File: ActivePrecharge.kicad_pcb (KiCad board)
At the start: 2 copper layers, 71 x 55 mm, 34 parts, among them Con1 LED, J1 Conn_01x03, J2 Conn_01x02, J3 Conn_01x02, Q1 IRLML0030, U1 NCP785AH50T1G, U2 NCP785AH50T1G, U3 TLV9301xDCK, U4 TCMT1106

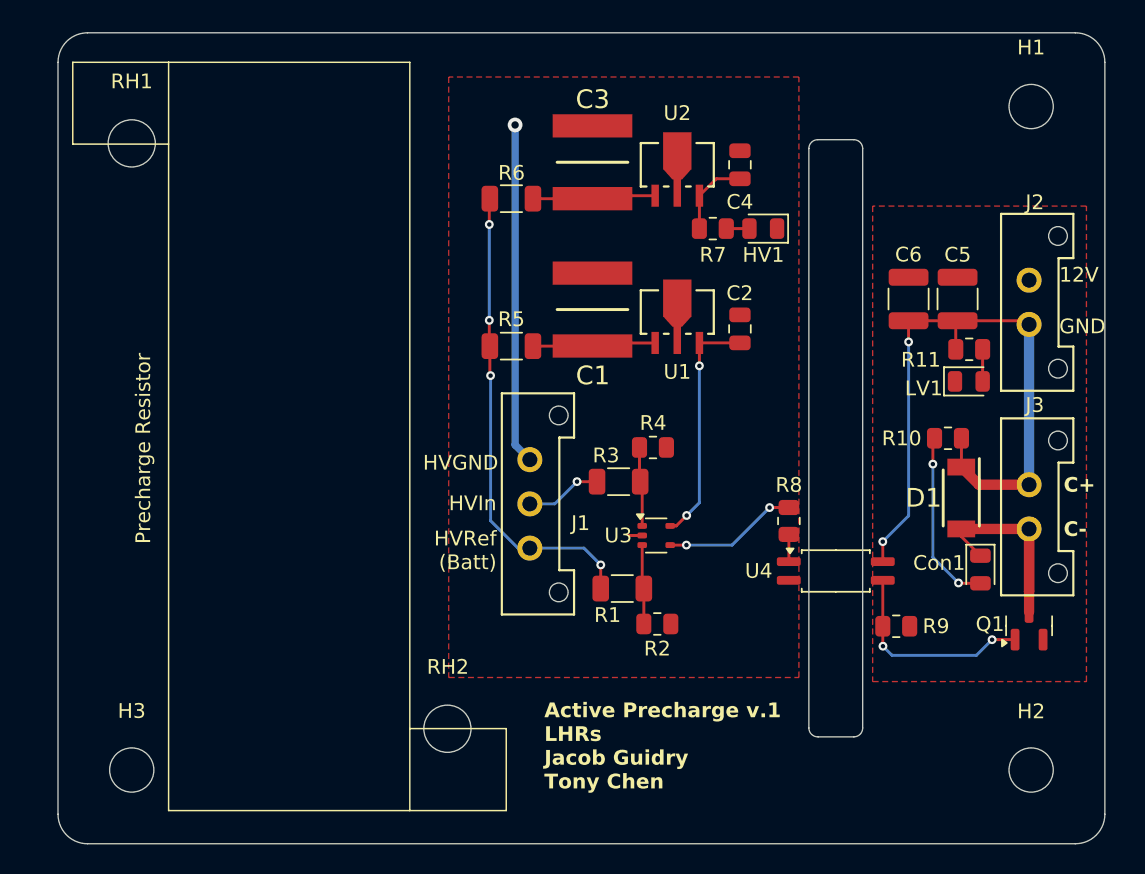
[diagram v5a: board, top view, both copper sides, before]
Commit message: refix HVGND isolation issue
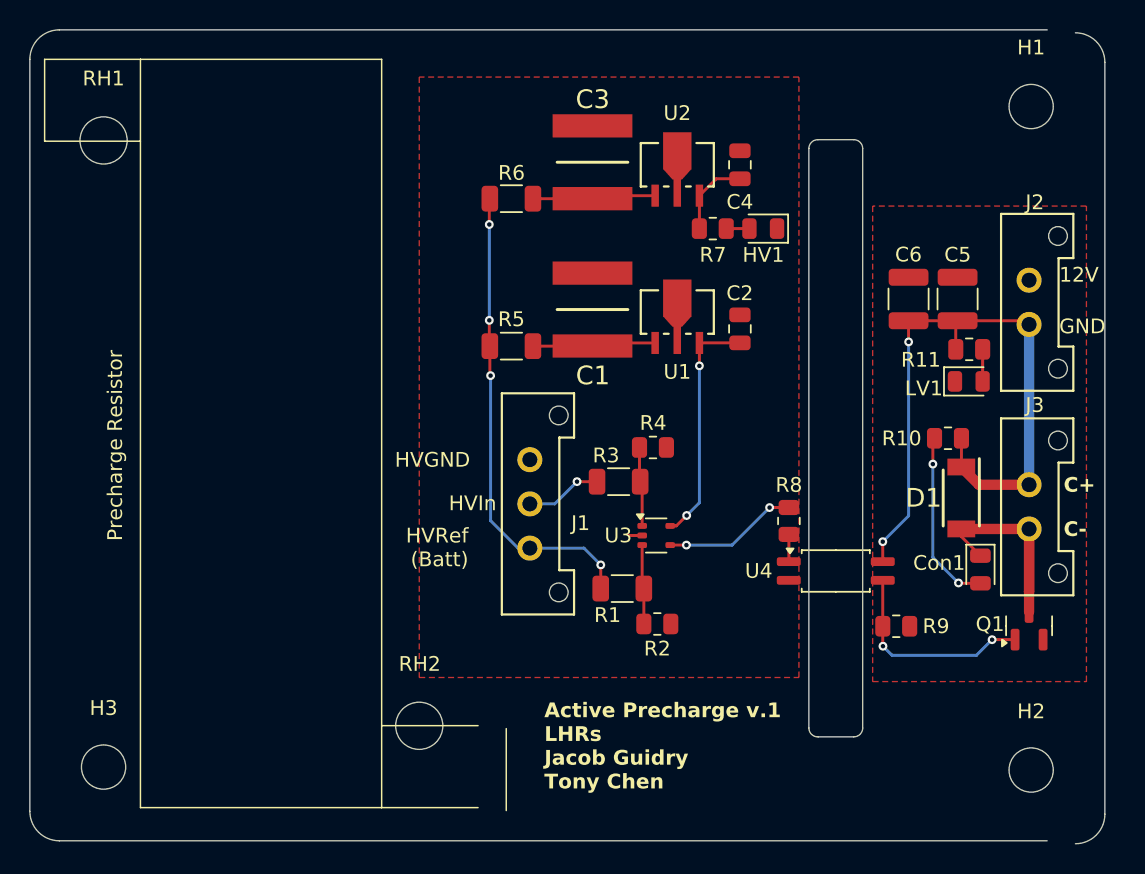
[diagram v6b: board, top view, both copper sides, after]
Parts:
- moved H3 1.92 mm to (77.6, 117.8)
- moved RH1 1.92 mm to (77.6, 75.3)
- moved RH2 1.92 mm to (99.0, 115.0)
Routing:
- net HVGND: track 24.0 -> 0.90 mm, vias 1 -> 0
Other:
- board size 71 x 55 mm -> 72.9 x 55.2 mm
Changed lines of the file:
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@@
 	(footprint "MountingHole:MountingHole_3mm"
 		(layer "F.Cu")
-		(at 79.5 118)
+		(at 77.59 117.8)
 		(descr "Mounting Hole 3mm, no annular")
 		(tags "mounting hole 3mm no annular")
@@
 	(footprint "MountingHole:MountingHole_3.2mm_M3"
 		(layer "F.Cu")
-		(at 100.91 115.2)
+		(at 99 115)
 		(descr "Mounting Hole 3.2mm, no annular, M3")
 		(tags "mounting hole 3.2mm no annular m3")
@@
 	(footprint "MountingHole:MountingHole_3.2mm_M3"
 		(layer "F.Cu")
-		(at 79.5 75.5)
+		(at 77.59 75.3)
 		(descr "Mounting Hole 3.2mm, no annular, M3")
 		(tags "mounting hole 3.2mm no annular m3")
@@
 	)
 	(gr_line
-		(start 98.36 120.75)
-		(end 82 120.75)
+		(start 96.45 120.55)
+		(end 80.09 120.55)
 		(stroke
 			(width 0.1)
@@
 	)
 	(gr_line
-		(start 82 70)
-		(end 75.5 70)
+		(start 80.09 69.8)
+		(end 73.59 69.8)
 		(stroke
 			(width 0.1)
@@
 	)
 	(gr_line
-		(start 75.5 75.55)
-		(end 82 75.55)
+		(start 73.59 75.35)
+		(end 80.09 75.35)
 		(stroke
 			(width 0.1)
@@
 	)
 	(gr_line
-		(start 98.36 120.75)
-		(end 104.9 120.75)
+		(start 96.45 120.55)
+		(end 102.99 120.55)
 		(stroke
 			(width 0.1)
@@
 	)
 	(gr_line
-		(start 75.5 70)
-		(end 75.5 75.55)
+		(start 73.59 69.8)
+		(end 73.59 75.35)
 		(stroke
 			(width 0.1)
@@
 	)
 	(gr_line
-		(start 98.36 70)
-		(end 98.36 120.75)
+		(start 96.45 69.8)
+		(end 96.45 120.55)
 		(stroke
 			(width 0.1)
@@
 	)
 	(gr_line
-		(start 104.9 115.19)
-		(end 98.36 115.19)
+		(start 102.99 114.99)
+		(end 96.45 114.99)
 		(stroke
 			(width 0.1)
@@
 	)
 	(gr_line
-		(start 82 70)
-		(end 98.36 70)
+		(start 80.09 69.8)
+		(end 96.45 69.8)
 		(stroke
 			(width 0.1)
@@
 	)
 	(gr_line
-		(start 82 120.75)
-		(end 82 70)
+		(start 80.09 120.55)
+		(end 80.09 69.8)
 		(stroke
 			(width 0.1)
@@
 	)
 	(gr_arc
-		(start 74.5 70)
-		(mid 75.085786 68.585786)
-		(end 76.5 68)
+		(start 72.59 69.8)
+		(mid 73.175786 68.385786)
+		(end 74.59 67.8)
 		(stroke
 			(width 0.05)
@@
 	)
 	(gr_arc
-		(start 76.5 123)
-		(mid 75.085786 122.414214)
-		(end 74.5 121)
+		(start 74.59 122.8)
+		(mid 73.175786 122.214214)
+		(end 72.59 120.8)
 		(stroke
 			(width 0.05)
@@
 	)
 	(gr_line
-		(start 143.5 123)
-		(end 76.5 123)
+		(start 141.59 122.8)
+		(end 74.59 122.8)
 		(stroke
 			(width 0.05)
@@
 	)
 	(gr_line
-		(start 76.5 68)
-		(end 143.5 68)
+		(start 74.59 67.8)
+		(end 141.59 67.8)
 		(stroke
 			(width 0.05)
@@
 	)
 	(gr_line
-		(start 74.5 121)
-		(end 74.5 70)
+		(start 72.59 120.8)
+		(end 72.59 69.8)
 		(stroke
 			(width 0.05)
@@
 	)
 	(gr_rect
-		(start 98.36 115.195)
-		(end 104.9 120.75)
+		(start 96.45 114.995)
+		(end 102.99 120.55)
 		(stroke
 			(width 0.1)
@@
 	)
 	(gr_line
-		(start 79.46 75.55)
-		(end 79.46 70)
+		(start 77.55 75.35)
+		(end 77.55 69.8)
 		(stroke
 			(width 0.1)
@@
 	)
 	(gr_line
-		(start 101.41 120.75)
-		(end 101.41 115.2)
+		(start 99 120.525)
+		(end 99 114.975)
 		(stroke
 			(width 0.1)
@@
 	)
 	(gr_rect
-		(start 82 70)
-		(end 98.36 120.75)
+		(start 80.09 69.8)
+		(end 96.45 120.55)
 		(stroke
 			(width 0.1)
@@
 	)
 	(gr_rect
-		(start 75.5 70)
-		(end 82 75.55)
+		(start 73.59 69.8)
+		(end 80.09 75.35)
 		(stroke
 			(width 0.1)
@@
 	)
 	(gr_text "HVRef\n(Batt)"
-		(at 104.25 104.5 0)
+		(at 102.34 104.3 0)
 		(layer "F.SilkS")
 		(effects
@@
 	)
 	(gr_text "Precharge Resistor"
-		(at 80.87 102.67 90)
+		(at 78.96 102.47 90)
 		(layer "F.SilkS")
 		(effects
@@
 	)
 	(gr_text "HVGND"
-		(at 99.25 97.75 0)
+		(at 97.34 97.55 0)
 		(layer "F.SilkS")
 		(effects
@@
 	)
 	(gr_text "Hypotenuse should be ~45.09\nfor legs 39.67 and 21.44"
-		(at 33 115.25 0)
+		(at 31.09 115.05 0)
 		(layer "User.1")
 		(effects
@@
 	)
 	(gr_text "Precharge Resistor"
-		(at 91.54 101.79 90)
+		(at 89.63 101.59 90)
 		(layer "User.1")
 		(effects
@@
 		(layer "User.1")
 		(pts
-			(xy 74.5 121) (xy 145.5 121)
+			(xy 72.59 120.8) (xy 143.59 120.8)
 		)
 		(height 15.75)
 		(gr_text "71.0000 mm"
-			(at 110 135.6 0)
+			(at 108.09 135.4 0)
 			(layer "User.1")
 			(effects
@@
 		(layer "User.1")
 		(pts
-			(xy 79.5 75.5) (xy 100.91 115.2)
+			(xy 77.59 75.3) (xy 99 115)
 		)
 		(height 38.290443)
 		(gr_text "45.1052 mm"
-			(at 57.51529 112.979388 298.3377502)
+			(at 55.60529 112.779388 298.3377502)
 			(layer "User.1")
 			(effects
@@
 		(layer "User.1")
 		(pts
-			(xy 79.5 118) (xy 74.5 118)
+			(xy 77.59 117.8) (xy 72.59 117.8)
 		)
 		(height 0)
 		(gr_text "5.0000 mm"
-			(at 77 116.85 0)
+			(at 75.09 116.65 0)
 			(layer "User.1")
 			(effects
@@
 		(layer "User.1")
 		(pts
-			(xy 79.5 75.5) (xy 79.5 118)
+			(xy 77.59 75.3) (xy 77.59 117.8)
 		)
 		(height 11.98)
 		(gr_text "42.5000 mm"
-			(at 66.37 96.75 90)
+			(at 64.46 96.55 90)
 			(layer "User.1")
 			(effects
@@
 		(layer "User.1")
 		(pts
-			(xy 79.5 118) (xy 79.5 123)
+			(xy 77.59 117.8) (xy 77.59 122.8)
 		)
 		(height 0)
 		(gr_text "5.0000 mm"
-			(at 78.35 120.5 90)
+			(at 76.44 120.3 90)
 			(layer "User.1")
 			(effects
@@
 		(layer "User.1")
 		(pts
-			(xy 79.5 118) (xy 140.5 118)
+			(xy 77.59 117.8) (xy 138.59 117.8)
 		)
 		(height 14.5)
 		(gr_text "61.0000 mm"
-			(at 110 131.35 0)
+			(at 108.09 131.15 0)
 			(layer "User.1")
 			(effects
@@
 		(net 3)
 	)
-	(via
-		(at 105.5 74.25)
-		(size 1)
-		(drill 0.5)
-		(layers "F.Cu" "B.Cu")
-		(free yes)
-		(net 3)
-	)
-	(segment
-		(start 105.5 74.25)
-		(end 105.5 95.95)
-		(width 0.5)
-		(layer "B.Cu")
-		(net 3)
-	)
-	(segment
-		(start 105.5 95.95)
-		(end 106.5 96.95)
-		(width 0.5)
-		(layer "B.Cu")
-		(net 3)
-	)
 	(segment
 		(start 122.765 100.195)
@@
 		(polygon
 			(pts
-				(xy 124.75 71) (xy 101 71) (xy 101 111.725) (xy 124.75 111.725)
+				(xy 124.75 71) (xy 99 71) (xy 99 111.725) (xy 124.75 111.725)
 			)
 		)
